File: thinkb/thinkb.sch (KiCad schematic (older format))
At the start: 127 parts, among them P1 battery+, P2 battery-, SW1 SW_Push, SW11 SW_Push, SW12 SW_Push, SW13 SW_Push, SW14 SW_Push, SW15 SW_Push, SW16 SW_Push, SW17 SW_Push, SW18 SW_Push, SW19 SW_Push, SW2 SW_Push, SW20 SW_Push, SW21 SW_Push, SW22 SW_Push, SW23 SW_Push, SW24 SW_Push, SW25 SW_Push, SW26 SW_Push, SW27 SW_Push, SW28 SW_Push, SW29 SW_Push, SW3 SW_Push, SW30 SW_Push, SW31 SW_Push, SW32 SW_Push, SW33 SW_Push, SW34 SW_Push, SW35 SW_Push, SW36 SW_Push, SW37 SW_Push, SW38 SW_Push, SW39 SW_Push, SW4 SW_Push, SW40 SW_Push, SW41 SW_Push, SW42 SW_Push, SW43 SW_Push, SW44 SW_Push, SW45 SW_Push, SW46 SW_Push, SW47 SW_Push, SW48 SW_Push, SW49 SW_Push, SW5 SW_Push, SW50 SW_Push, SW51 SW_Push, SW52 SW_Push, SW53 SW_Push, SW54 SW_Push, SW55 SW_Push, SW56 SW_Push, SW57 SW_Push, SW58 SW_Push, SW59 SW_Push, SW6 SW_Push, SW60 SW_Push, SW61 SW_Push, SW62 Reset, SW63 Power, SW7 SW_Push, SW8 SW_Push, SW9 SW_Push

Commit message: WIP
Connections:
- net GND: now also MCU1.23 (GND), P2.1 (Pin_1)
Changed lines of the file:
@@
 Wire Wire Line
 	9150 3800 8600 3800
+Text GLabel 9600 4150 2    50   Input ~ 0
+GND
+Wire Wire Line
+	9600 4150 9550 4150
+Wire Wire Line
+	9550 4150 9550 4000
+Connection ~ 9550 4000
 $EndSCHEMATC

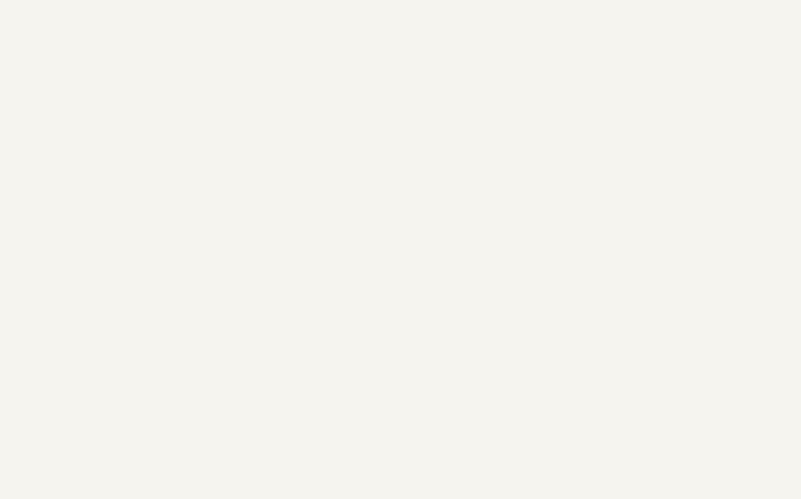
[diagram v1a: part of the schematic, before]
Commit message: Mounting holes
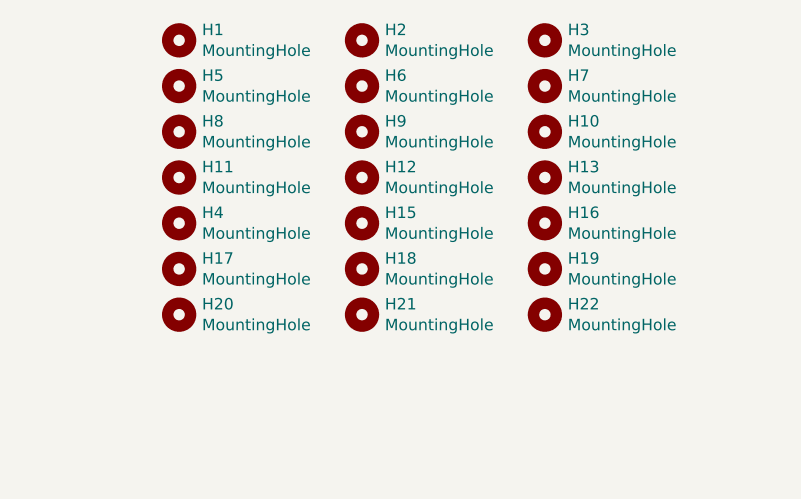
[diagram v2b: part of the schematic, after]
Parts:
- added H1, H10, H11, H12, H13, H15, H16, H17, H18, H19, H2, H20, H21, H22, H3, H4, H5, H6, H7, H8, H9: MountingHole, MountingHole:MountingHole_2.2mm_M2, symbol Mechanical:MountingHole
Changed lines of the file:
@@
 	9550 4150 9550 4000
 Connection ~ 9550 4000
+$Comp
+L Mechanical:MountingHole H1
+U 1 1 6153F96B
+P 7600 950
+F 0 "H1" H 7700 996 50  0000 L CNN
+F 1 "MountingHole" H 7700 905 50  0000 L CNN
+F 2 "MountingHole:MountingHole_2.2mm_M2" H 7600 950 50  0001 C CNN
+F 3 "~" H 7600 950 50  0001 C CNN
+	1    7600 950
+	1    0    0    -1
+$EndComp
+$Comp
+L Mechanical:MountingHole H5
+U 1 1 61545B9C
+P 7600 1150
+F 0 "H5" H 7700 1196 50  0000 L CNN
+F 1 "MountingHole" H 7700 1105 50  0000 L CNN
+F 2 "MountingHole:MountingHole_2.2mm_M2" H 7600 1150 50  0001 C CNN
+F 3 "~" H 7600 1150 50  0001 C CNN
+	1    7600 1150
+	1    0    0    -1
+$EndComp
+$Comp
+L Mechanical:MountingHole H8
+U 1 1 6154A57C
+P 7600 1350
+F 0 "H8" H 7700 1396 50  0000 L CNN
+F 1 "MountingHole" H 7700 1305 50  0000 L CNN
+F 2 "MountingHole:MountingHole_2.2mm_M2" H 7600 1350 50  0001 C CNN
+F 3 "~" H 7600 1350 50  0001 C CNN
+	1    7600 1350
+	1    0    0    -1
+$EndComp
+$Comp
+L Mechanical:MountingHole H11
+U 1 1 6154EEAB
+P 7600 1550
+F 0 "H11" H 7700 1596 50  0000 L CNN
+F 1 "MountingHole" H 7700 1505 50  0000 L CNN
+F 2 "MountingHole:MountingHole_2.2mm_M2" H 7600 1550 50  0001 C CNN
+F 3 "~" H 7600 1550 50  0001 C CNN
+	1    7600 1550
+	1    0    0    -1
+$EndComp
+$Comp
+L Mechanical:MountingHole H17
+U 1 1 6155803C
+P 7600 1950
+F 0 "H17" H 7700 1996 50  0000 L CNN
+F 1 "MountingHole" H 7700 1905 50  0000 L CNN
+F 2 "MountingHole:MountingHole_2.2mm_M2" H 7600 1950 50  0001 C CNN
+F 3 "~" H 7600 1950 50  0001 C CNN
+	1    7600 1950
+	1    0    0    -1
+$EndComp
+$Comp
+L Mechanical:MountingHole H20
+U 1 1 6155DE5B
+P 7600 2150
+F 0 "H20" H 7700 2196 50  0000 L CNN
+F 1 "MountingHole" H 7700 2105 50  0000 L CNN
+F 2 "MountingHole:MountingHole_2.2mm_M2" H 7600 2150 50  0001 C CNN
+F 3 "~" H 7600 2150 50  0001 C CNN
+	1    7600 2150
+	1    0    0    -1
+$EndComp
+$Comp
+L Mechanical:MountingHole H2
+U 1 1 6158B5E4
+P 8400 950
+F 0 "H2" H 8500 996 50  0000 L CNN
+F 1 "MountingHole" H 8500 905 50  0000 L CNN
+F 2 "MountingHole:MountingHole_2.2mm_M2" H 8400 950 50  0001 C CNN
+F 3 "~" H 8400 950 50  0001 C CNN
+	1    8400 950
+	1    0    0    -1
+$EndComp
+$Comp
+L Mechanical:MountingHole H6
+U 1 1 6158B5EA
+P 8400 1150
+F 0 "H6" H 8500 1196 50  0000 L CNN
+F 1 "MountingHole" H 8500 1105 50  0000 L CNN
+F 2 "MountingHole:MountingHole_2.2mm_M2" H 8400 1150 50  0001 C CNN
+F 3 "~" H 8400 1150 50  0001 C CNN
+	1    8400 1150
+	1    0    0    -1
+$EndComp
+$Comp
+L Mechanical:MountingHole H9
+U 1 1 6158B5F0
+P 8400 1350
+F 0 "H9" H 8500 1396 50  0000 L CNN
+F 1 "MountingHole" H 8500 1305 50  0000 L CNN
+F 2 "MountingHole:MountingHole_2.2mm_M2" H 8400 1350 50  0001 C CNN
+F 3 "~" H 8400 1350 50  0001 C CNN
+	1    8400 1350
+	1    0    0    -1
+$EndComp
+$Comp
+L Mechanical:MountingHole H12
+U 1 1 6158B5F6
+P 8400 1550
+F 0 "H12" H 8500 1596 50  0000 L CNN
+F 1 "MountingHole" H 8500 1505 50  0000 L CNN
+F 2 "MountingHole:MountingHole_2.2mm_M2" H 8400 1550 50  0001 C CNN
+F 3 "~" H 8400 1550 50  0001 C CNN
+	1    8400 1550
+	1    0    0    -1
+$EndComp
+$Comp
+L Mechanical:MountingHole H15
+U 1 1 6158B5FC
+P 8400 1750
+F 0 "H15" H 8500 1796 50  0000 L CNN
+F 1 "MountingHole" H 8500 1705 50  0000 L CNN
+F 2 "MountingHole:MountingHole_2.2mm_M2" H 8400 1750 50  0001 C CNN
+F 3 "~" H 8400 1750 50  0001 C CNN
+	1    8400 1750
+	1    0    0    -1
+$EndComp
+$Comp
+L Mechanical:MountingHole H18
+U 1 1 6158B602
+P 8400 1950
+F 0 "H18" H 8500 1996 50  0000 L CNN
+F 1 "MountingHole" H 8500 1905 50  0000 L CNN
+F 2 "MountingHole:MountingHole_2.2mm_M2" H 8400 1950 50  0001 C CNN
+F 3 "~" H 8400 1950 50  0001 C CNN
+	1    8400 1950
+	1    0    0    -1
+$EndComp
+$Comp
+L Mechanical:MountingHole H21
+U 1 1 6158B608
+P 8400 2150
+F 0 "H21" H 8500 2196 50  0000 L CNN
+F 1 "MountingHole" H 8500 2105 50  0000 L CNN
+F 2 "MountingHole:MountingHole_2.2mm_M2" H 8400 2150 50  0001 C CNN
+F 3 "~" H 8400 2150 50  0001 C CNN
+	1    8400 2150
+	1    0    0    -1
+$EndComp
+$Comp
+L Mechanical:MountingHole H3
+U 1 1 61591EB2
+P 9200 950
+F 0 "H3" H 9300 996 50  0000 L CNN
+F 1 "MountingHole" H 9300 905 50  0000 L CNN
+F 2 "MountingHole:MountingHole_2.2mm_M2" H 9200 950 50  0001 C CNN
+F 3 "~" H 9200 950 50  0001 C CNN
+	1    9200 950
+	1    0    0    -1
+$EndComp
+$Comp
+L Mechanical:MountingHole H7
+U 1 1 61591EB8
+P 9200 1150
+F 0 "H7" H 9300 1196 50  0000 L CNN
+F 1 "MountingHole" H 9300 1105 50  0000 L CNN
+F 2 "MountingHole:MountingHole_2.2mm_M2" H 9200 1150 50  0001 C CNN
+F 3 "~" H 9200 1150 50  0001 C CNN
+	1    9200 1150
+	1    0    0    -1
+$EndComp
+$Comp
+L Mechanical:MountingHole H10
+U 1 1 61591EBE
+P 9200 1350
+F 0 "H10" H 9300 1396 50  0000 L CNN
+F 1 "MountingHole" H 9300 1305 50  0000 L CNN
+F 2 "MountingHole:MountingHole_2.2mm_M2" H 9200 1350 50  0001 C CNN
+F 3 "~" H 9200 1350 50  0001 C CNN
+	1    9200 1350
+	1    0    0    -1
+$EndComp
+$Comp
+L Mechanical:MountingHole H13
+U 1 1 61591EC4
+P 9200 1550
+F 0 "H13" H 9300 1596 50  0000 L CNN
+F 1 "MountingHole" H 9300 1505 50  0000 L CNN
+F 2 "MountingHole:MountingHole_2.2mm_M2" H 9200 1550 50  0001 C CNN
+F 3 "~" H 9200 1550 50  0001 C CNN
+	1    9200 1550
+	1    0    0    -1
+$EndComp
+$Comp
+L Mechanical:MountingHole H16
+U 1 1 61591ECA
+P 9200 1750
+F 0 "H16" H 9300 1796 50  0000 L CNN
+F 1 "MountingHole" H 9300 1705 50  0000 L CNN
+F 2 "MountingHole:MountingHole_2.2mm_M2" H 9200 1750 50  0001 C CNN
+F 3 "~" H 9200 1750 50  0001 C CNN
+	1    9200 1750
+	1    0    0    -1
+$EndComp
+$Comp
+L Mechanical:MountingHole H19
+U 1 1 61591ED0
+P 9200 1950
+F 0 "H19" H 9300 1996 50  0000 L CNN
+F 1 "MountingHole" H 9300 1905 50  0000 L CNN
+F 2 "MountingHole:MountingHole_2.2mm_M2" H 9200 1950 50  0001 C CNN
+F 3 "~" H 9200 1950 50  0001 C CNN
+	1    9200 1950
+	1    0    0    -1
+$EndComp
+$Comp
+L Mechanical:MountingHole H22
+U 1 1 61591ED6
+P 9200 2150
+F 0 "H22" H 9300 2196 50  0000 L CNN
+F 1 "MountingHole" H 9300 2105 50  0000 L CNN
+F 2 "MountingHole:MountingHole_2.2mm_M2" H 9200 2150 50  0001 C CNN
+F 3 "~" H 9200 2150 50  0001 C CNN
+	1    9200 2150
+	1    0    0    -1
+$EndComp
+$Comp
+L Mechanical:MountingHole H4
+U 1 1 6159B775
+P 7600 1750
+F 0 "H4" H 7700 1796 50  0000 L CNN
+F 1 "MountingHole" H 7700 1705 50  0000 L CNN
+F 2 "MountingHole:MountingHole_2.2mm_M2" H 7600 1750 50  0001 C CNN
+F 3 "~" H 7600 1750 50  0001 C CNN
+	1    7600 1750
+	1    0    0    -1
+$EndComp
 $EndSCHEMATC

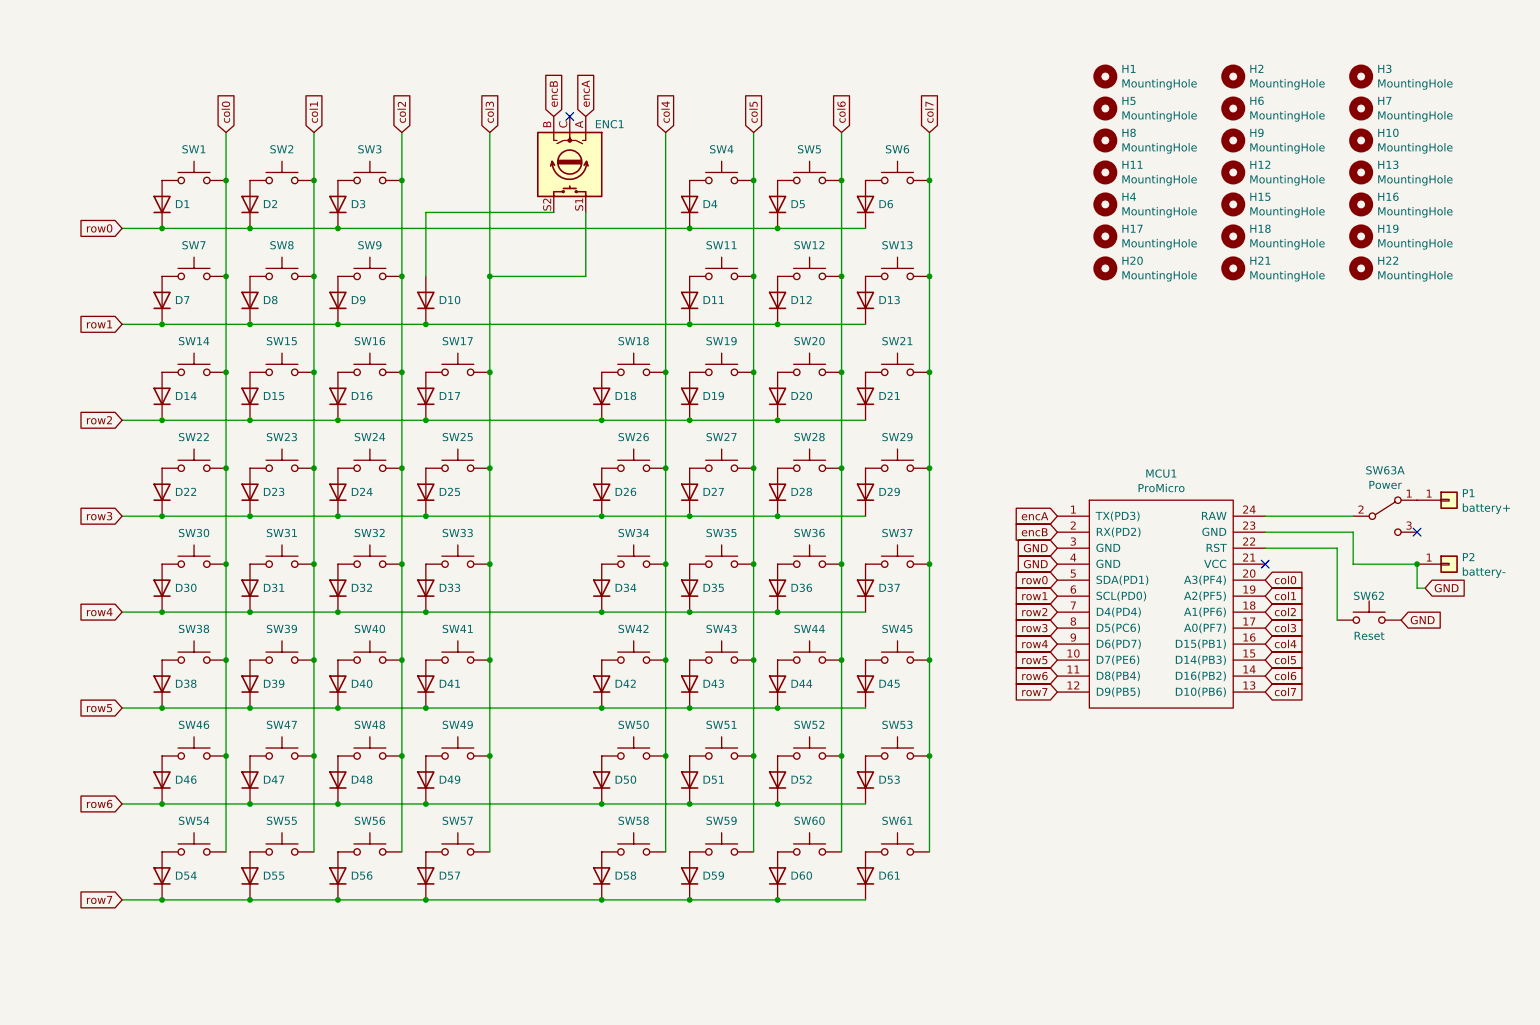
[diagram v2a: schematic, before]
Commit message: Added horizontal encoder to the schema
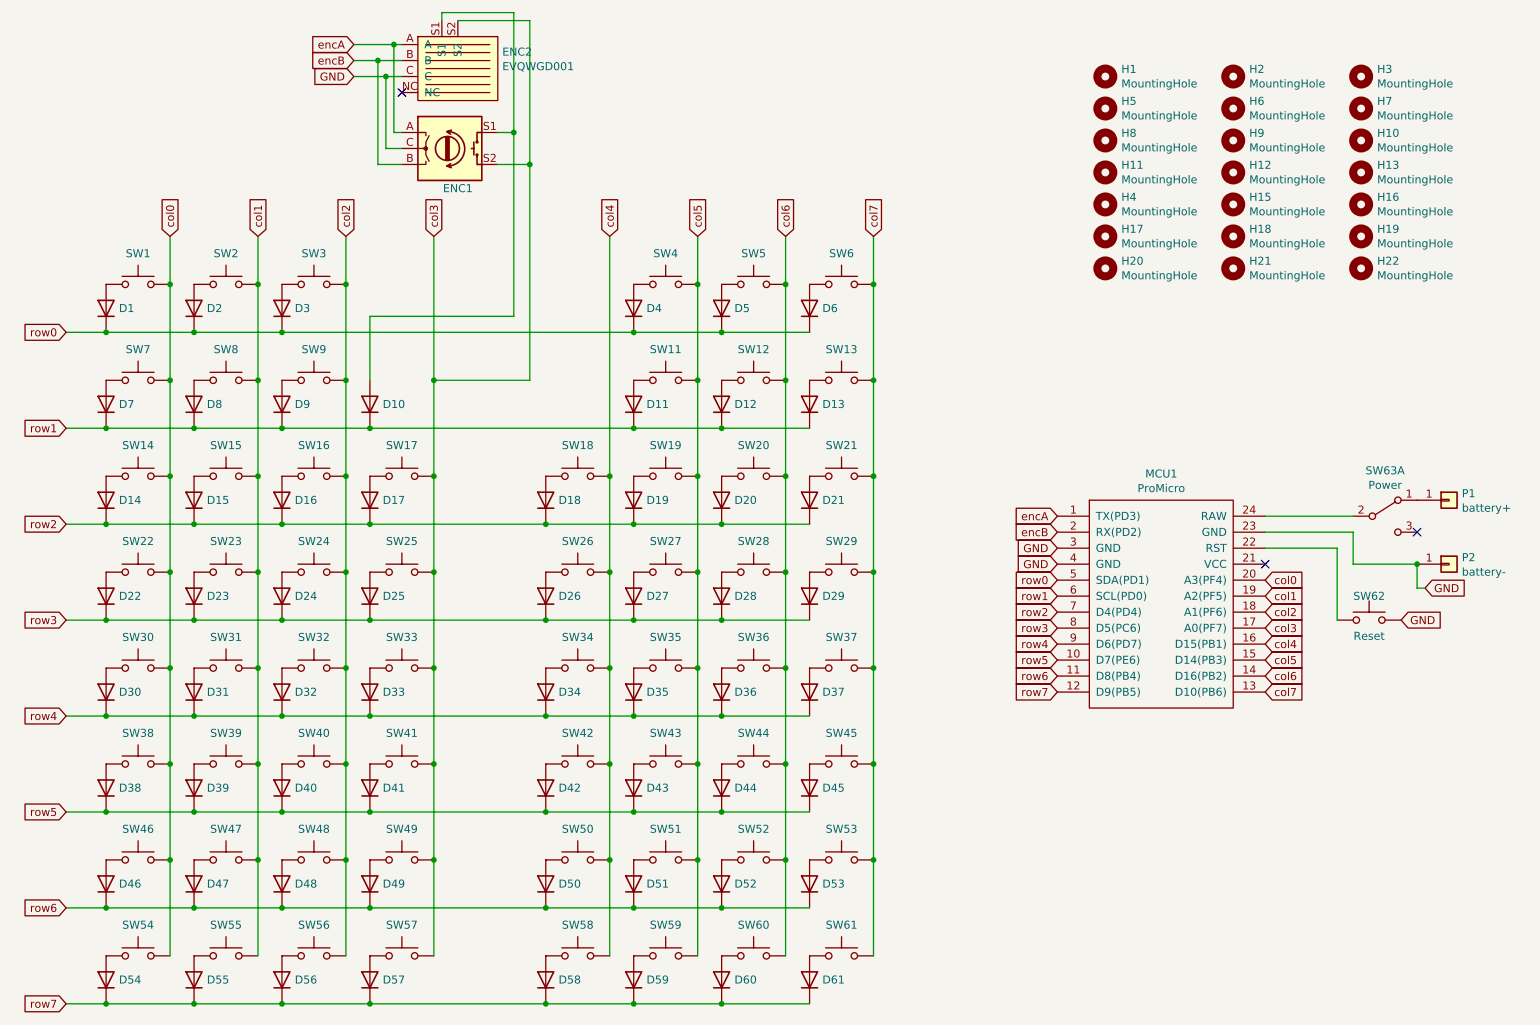
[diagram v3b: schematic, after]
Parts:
- added ENC2: EVQWGD001, footprints:RollerEncoder_Panasonic_EVQWGD001, symbol evqwgd001:EVQWGD001
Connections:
- net GND: now also ENC1.C, ENC2.C
- net col3: now also ENC1.S2, ENC2.S2; no longer ENC1.S1
- net encA: now also ENC2.A
- net encB: now also ENC2.B
- net at D10.2 (A): now also ENC1.S1, ENC2.S1; no longer ENC1.S2
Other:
- moved on the sheet: D1, D10, D11, D12, D13, D14, D15, D16, D17, D18, D19, D2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

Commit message: WIP
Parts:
- ENC2: footprint footprints:RollerEncoder_Panasonic_EVQWGD001 -> footprints:EVQWGD001
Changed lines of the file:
@@
 F 0 "ENC2" H 3828 904 50  0000 L CNN
 F 1 "EVQWGD001" H 3828 813 50  0000 L CNN
-F 2 "footprints:RollerEncoder_Panasonic_EVQWGD001" H 3550 850 50  0001 C CNN
+F 2 "footprints:EVQWGD001" H 3550 850 50  0001 C CNN
 F 3 "" H 3550 850 50  0001 C CNN
 	1    3550 850

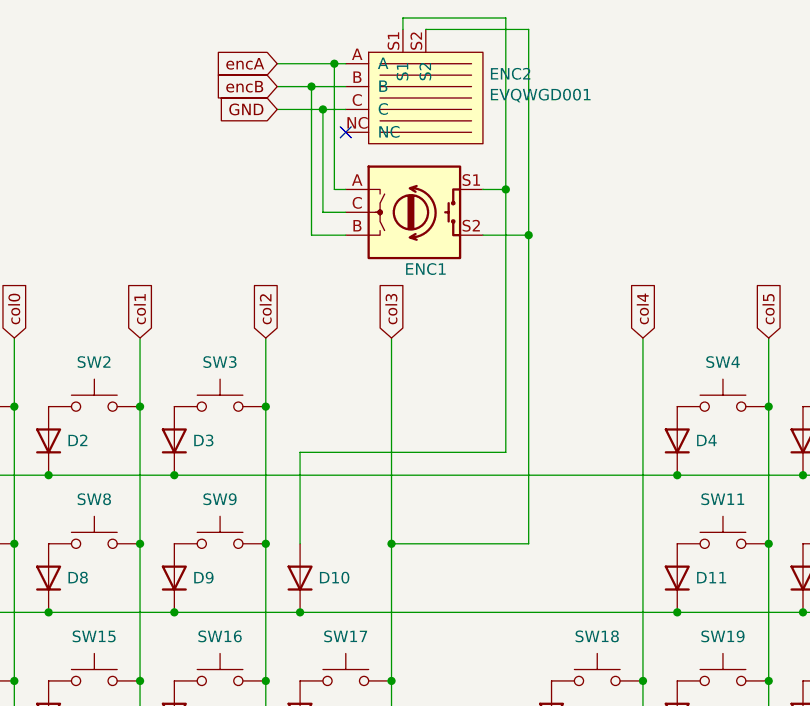
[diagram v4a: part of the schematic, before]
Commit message: Horizontal encoder
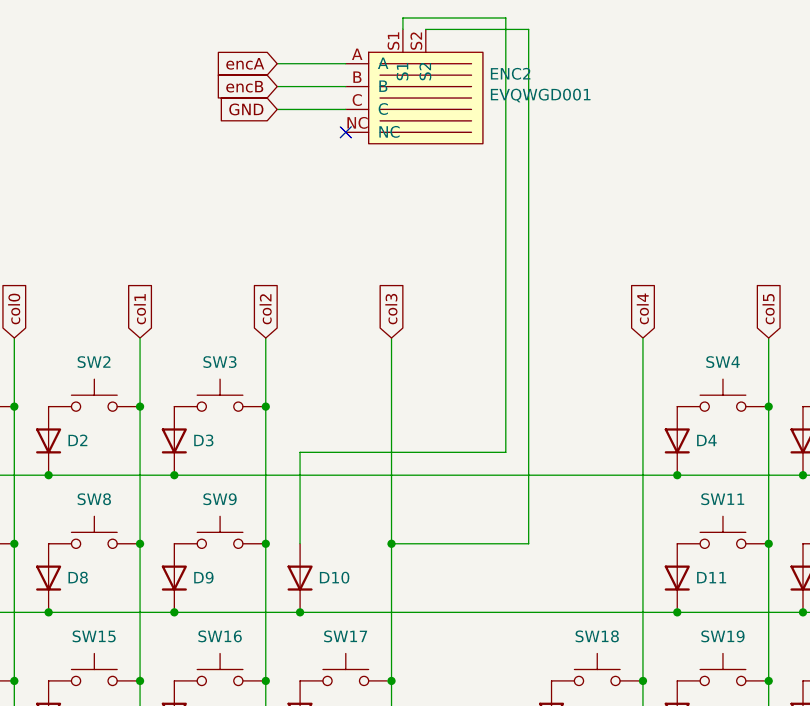
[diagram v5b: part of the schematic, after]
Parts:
- removed ENC1: Rotary_Encoder_Switch, footprints:RotaryEncoder_Alps_EC11E, symbol Device:Rotary_Encoder_Switch
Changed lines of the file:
@@
 Wire Wire Line
 	3400 1950 3400 2850
-$Comp
-L Device:Rotary_Encoder_Switch ENC1
-U 1 1 616135F5
-P 3500 1400
-F 0 "ENC1" H 3550 1150 50  0000 C CNN
-F 1 "Rotary_Encoder_Switch" V 3250 2000 50  0001 C CNN
-F 2 "footprints:RotaryEncoder_Alps_EC11E" H 3350 1560 50  0001 C CNN
-F 3 "~" H 3500 1660 50  0001 C CNN
-	1    3500 1400
-	1    0    0    -1
-$EndComp
 Text GLabel 2900 850  0    50   Input ~ 0
 encB
@@
 GND
 Wire Wire Line
-	3200 750  3150 750
-Wire Wire Line
-	3200 850  3050 850
-Wire Wire Line
-	3200 950  3100 950
-Wire Wire Line
-	3200 1300 3150 1300
-Wire Wire Line
-	3150 1300 3150 750
-Connection ~ 3150 750
-Wire Wire Line
-	3150 750  2900 750
-Wire Wire Line
-	3200 1400 3100 1400
-Wire Wire Line
-	3100 1400 3100 950
-Connection ~ 3100 950
-Wire Wire Line
-	3100 950  2900 950
-Wire Wire Line
-	3200 1500 3050 1500
-Wire Wire Line
-	3050 1500 3050 850
-Connection ~ 3050 850
-Wire Wire Line
-	3050 850  2900 850
-Wire Wire Line
 	3550 600  4000 600
 Wire Wire Line
-	4000 600  4000 1500
-Wire Wire Line
-	4000 1500 3800 1500
-Wire Wire Line
 	3450 600  3450 550
 Wire Wire Line
 	3450 550  3900 550
 Wire Wire Line
-	3900 550  3900 1300
-Wire Wire Line
-	3900 1300 3800 1300
-Wire Wire Line
-	4000 1500 4000 2850
-Connection ~ 4000 1500
-Wire Wire Line
-	3900 1300 3900 2450
-Wire Wire Line
 	3000 2450 3900 2450
-Connection ~ 3900 1300
 $Comp
 L Mechanical:MountingHole H21
@@
 $EndComp
 NoConn ~ 3200 1050
+Wire Wire Line
+	3900 550  3900 2450
+Wire Wire Line
+	4000 600  4000 2850
+Wire Wire Line
+	2900 850  3200 850
+Wire Wire Line
+	2900 950  3200 950
+Wire Wire Line
+	2900 750  3200 750
 $EndSCHEMATC

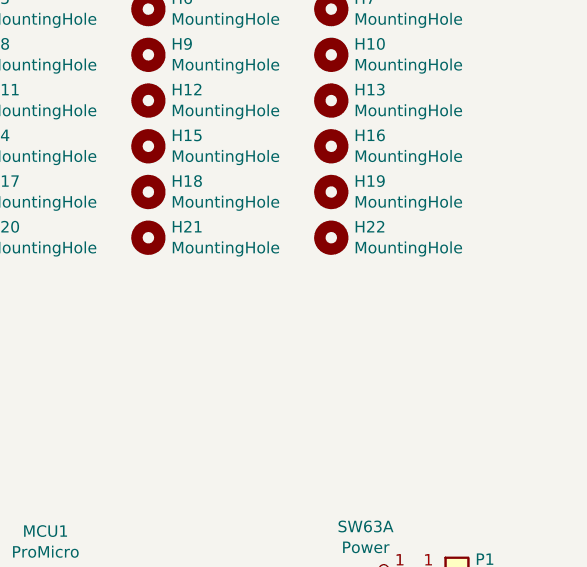
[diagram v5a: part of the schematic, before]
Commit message: Moving mounting holes
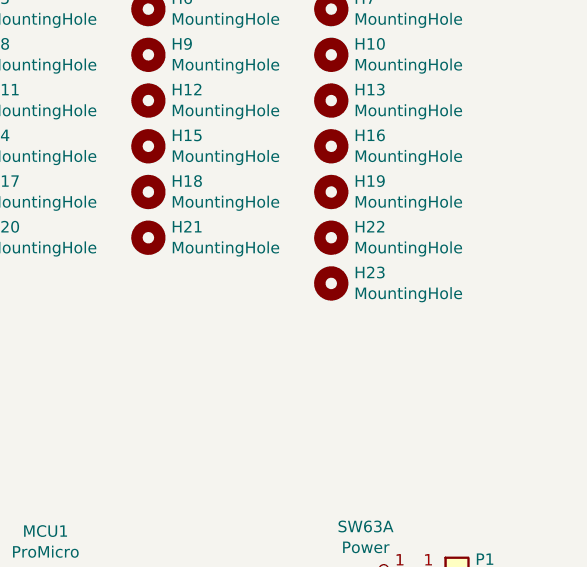
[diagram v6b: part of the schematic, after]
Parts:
- added H23: MountingHole, MountingHole:MountingHole_2.2mm_M2, symbol Mechanical:MountingHole
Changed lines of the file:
@@
 Wire Wire Line
 	2900 750  3200 750
+$Comp
+L Mechanical:MountingHole H23
+U 1 1 61621F0C
+P 9200 2350
+F 0 "H23" H 9300 2396 50  0000 L CNN
+F 1 "MountingHole" H 9300 2305 50  0000 L CNN
+F 2 "MountingHole:MountingHole_2.2mm_M2" H 9200 2350 50  0001 C CNN
+F 3 "~" H 9200 2350 50  0001 C CNN
+	1    9200 2350
+	1    0    0    -1
+$EndComp
 $EndSCHEMATC
